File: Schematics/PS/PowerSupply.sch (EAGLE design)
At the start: 32 parts, among them Q1 BUZ10, Q2 BUZ10

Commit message: updates to PS schematic
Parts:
- removed Q1, Q2: BUZ10, transistor-fet:BUZ10
- added C4: (no value), resistor:C-EU025-050X050
- added D6, D7: 1N4933, diode:1N4933
- added R12: (no value), resistor:R-US_0617/22
- added R13, R14: (no value), resistor:R-US_0204/2V
- added T1, T2: IRFP240, Amplifier_Parts:IRFP240
- added TRAFO1: COIL_FORMER, Amplifier_Parts:COIL_FORMER
- R5: device resistor:R-US_0309/12 -> resistor:R-US_0617/22
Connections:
- removed net N$13 (its old number): C1.1, U$5.COM
- new net N$19: D6.C, R13.2, T1.G
- new net N$20: D7.A, R14.1, U$5.LO
- new net N$21: D7.C, R14.2, T2.G
- new net N$22: C2.1, T1.S, T2.D, TRAFO1.P1, U$5.VS
- new net N$9: C4.2, D5.A, R4.1, U$5.VCC
- net N$14: now also D6.A, R13.1, U$5.HO; no longer C2.1, U$5.VS
- net N$4: now also C3.1, R12.2, R4.2, R5.2, U$6.+; no longer D5.A, R4.1, U$5.VCC
- net PE: now also C1.1, C3.2, C4.1, R12.1, R5.1, TRAFO1.P15, TRAFO1.P2, U$5.COM, U$6.-
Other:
- moved on the sheet: C1, C2, D5, R3, R4

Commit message: updates to PS, libary and Action items
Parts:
- removed C16: 1uF, rcl:C-EU025-060X050
- removed D5: 1N4933, diode:1N4933
- removed R12: (no value), resistor:R-US_0617/22
- added C5: 330uF, rcl:CPOL-USE7.5-18
- added R15: 47k, rcl:R-US_0617/5V
- C1, C2: device resistor:C-EU025-050X050 -> rcl:C-EU050-035X075
- C15: device rcl:C-EU025-060X050 -> rcl:C-EU102-064X133
- C17: device rcl:C-EU025-060X050 -> rcl:C-EU075-042X103
- C3: value (none) -> 1uF; device resistor:C-US050-050X075 -> rcl:C-EU102-064X133
- C4: value (none) -> 100uF; device resistor:C-EU025-050X050 -> rcl:CPOL-EUE2.5-6
- D2: value 22V -> 25V; device diode:ZENER-DIODEP1-12 -> diode:ZENER-DIODEP1-Z12
- D3: device diode:ZENER-DIODEDO34-7 -> diode:ZENER-DIODEZD-2.5
- D4: device diode:ZENER-DIODEP1-12 -> diode:ZENER-DIODEP1-Z12
- L1: value RKZ4 -> CHOKE; device inductors:RKZ4 -> Amplifier_Parts:CHOKE
- R1, R7, R8: device resistor:R-US_0207/15 -> rcl:R-US_0204/2V
- R10, R11, R9: device rcl:R-US_0617/22 -> rcl:R-US_0617/5V
- R3: device resistor:R-US_0309/10 -> rcl:R-US_0204/2V
- R4: value (none) -> 47k; device resistor:R-US_0309/10 -> rcl:R-US_0617/5V
- R5: value (none) -> 47k; device resistor:R-US_0617/22 -> rcl:R-US_0617/5V
- R6: device resistor:R-US_0207/15 -> rcl:R-US_0309/V
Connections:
- removed net N$4 (its old number): C3.1, R12.2, R4.2, R5.2, U$6.+
- removed net N$8: C17.2, R10.2, R11.2, R9.2, U$1.NO
- removed net VAC-: C17.1, R10.1, R11.1, R9.1, U$1.COM
- new net N$17: C4.+, R5.1, U$5.VCC
- new net N$24: TRAFO1.S30+1, TRAFO1.SEC30V+
- new net N$25: TRAFO1.GND30
- new net N$26: TRAFO1.S15+1, TRAFO1.SEC15+
- new net N$27: TRAFO1.S15-1, TRAFO1.SEC15-
- new net N$28: TRAFO1.GND15
- new net V+: C5.+, R15.2, R4.2, R5.2, T1.D, U$6.+
- net GND: now also C1.1, C17.1, C5.-, L1.W2E, R10.1, R11.1, R15.1, R4.1, R9.1, T2.S, TRAFO1.P2, TRAFO1.P22, TRAFO1.P23, TRAFO1.P24, TRAFO1.P25, U$1.COM, U$5.COM, U$6.-; no longer C16.2
- net N$10: now also C3.1; no longer C16.1
- net N$14: now also D6.C; no longer D6.A
- net N$18: now also C17.2, R10.2, R11.2, R9.2, U$1.NO; no longer L1.W2E
- net N$19: now also D6.A; no longer D6.C
- net N$20: now also D7.C; no longer D7.A
- net N$21: now also D7.A; no longer D7.C
- net N$22: now also TRAFO1.P12, TRAFO1.P13, TRAFO1.P14, TRAFO1.P15
- net N$6: no longer D5.C
- net N$9: now also TRAFO1.S30-1, TRAFO1.SEC30-; no longer C4.2, D5.A, R4.1, U$5.VCC
- net PE: no longer C1.1, C4.1, R12.1, R5.1, TRAFO1.P15, TRAFO1.P2, U$5.COM, U$6.-
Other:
- note added: "Vac+"
- note added: "check this FP"
- note added: "to mute"
- note removed: "Slow Start Up"
- note removed: "resevoir capacitor - need to decide on value (maybe we can use many in parallel) bledder resistor -we can use the same as the old power supply"
- moved on the sheet: C15, C17, C2, C3, D1, D2, D3, D4, D6, D7, LED2, R1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

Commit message: PS schem updates
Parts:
- added C10, C7, C8, C9: 0.1uF, rcl:C-EU102-064X133
- added C11, C12: 1uF, rcl:C-EU102-064X133
- added C13, C19: 15,000uF, Amplifier_Parts:LNR1K153MSE
- added D10, D5, D8, D9: VS-ETL1506-M3, Amplifier_Parts:VS-ETL1506-M3
- added R12: 100, resistor:R-US_0207/15
- added R16: 2k, rcl:R-US_VTA52
- added R17, R18: 1, rcl:R-US_0411/12
- R2: value 100 -> 2k; device resistor:R-US_0207/15 -> rcl:R-US_VTA52
- R6: value 560 -> 330
- R7: value 390 -> 33; device rcl:R-US_0204/2V -> rcl:R-US_0309/V
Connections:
- net N$24 renamed VAC+40
- net N$26 renamed VAC+15
- net N$27 renamed VAC-15
- net N$9 renamed VAC-40
- removed net N$25: TRAFO1.GND30
- removed net N$28: TRAFO1.GND15
- new net N$23: D5.NC@2, D8.NC@1
- new net N$24: D10.C, D9.A
- new net N$8: C9.2, R17.2
- new net N$9: D5.A, D8.C
- new net SGND: C10.1, C11.2, C12.1, C13.+, C19.-, C7.2, C8.1, R12.1, R16.2, R17.1, R2.1, TRAFO1.GND15, TRAFO1.GND30
- new net VEE: C12.2, C13.-, C8.2, D10.A, D8.A, R16.1, R18.1
- net GND: now also R12.2; no longer R2.1
- net N$10: now also R7.1; no longer R7.2
- net N$11: now also R7.2; no longer R7.1
- net N$3: now also C10.2, R18.2; no longer R2.2, U$3.S2
- net VCC: now also C11.1, C19.+, C7.1, C9.1, D5.C, D9.C, R2.2
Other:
- note added: "check FP"
- note removed: "* we may possibly add the diode bridge rectifier here for the SMPS"
- note removed: "check this FP"
- moved on the sheet: R2, R7, U$3

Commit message: updates to PS
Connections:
- removed net N$24: D10.C, D9.A
- removed net N$9: D5.A, D8.C
- net VAC+40: now also D5.A, D8.C
- net VAC-40: now also D10.C, D9.A
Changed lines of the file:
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@@
 <junction x="177.8" y="60.96"/>
+</segment>
+<segment>
+<pinref part="D5" gate="G$1" pin="A"/>
+<wire x1="88.9" y1="22.86" x2="83.82" y2="22.86" width="0.1524" layer="91"/>
+<pinref part="D8" gate="G$1" pin="C"/>
+<wire x1="83.82" y1="22.86" x2="63.5" y2="22.86" width="0.1524" layer="91"/>
+<wire x1="83.82" y1="20.32" x2="83.82" y2="22.86" width="0.1524" layer="91"/>
+<junction x="83.82" y="22.86"/>
 </segment>
 </net>
@@
 <wire x1="182.88" y1="53.34" x2="177.8" y2="53.34" width="0.1524" layer="91"/>
 <junction x="177.8" y="53.34"/>
+</segment>
+<segment>
+<wire x1="63.5" y1="10.16" x2="99.06" y2="10.16" width="0.1524" layer="91"/>
+<pinref part="D9" gate="G$1" pin="A"/>
+<wire x1="99.06" y1="10.16" x2="99.06" y2="12.7" width="0.1524" layer="91"/>
+<wire x1="99.06" y1="15.24" x2="99.06" y2="12.7" width="0.1524" layer="91"/>
+<pinref part="D10" gate="G$1" pin="C"/>
+<wire x1="99.06" y1="12.7" x2="93.98" y2="12.7" width="0.1524" layer="91"/>
+<junction x="99.06" y="12.7"/>
 </segment>
 </net>
@@
 <wire x1="83.82" y1="-17.78" x2="106.68" y2="-17.78" width="0.1524" layer="91"/>
 <junction x="106.68" y="-17.78"/>
+<junction x="83.82" y="12.7"/>
 </segment>
 </net>
@@
 </segment>
 </net>
-<net name="N$9" class="0">
-<segment>
-<pinref part="D5" gate="G$1" pin="A"/>
-<wire x1="88.9" y1="22.86" x2="83.82" y2="22.86" width="0.1524" layer="91"/>
-<pinref part="D8" gate="G$1" pin="C"/>
-<wire x1="83.82" y1="22.86" x2="63.5" y2="22.86" width="0.1524" layer="91"/>
-<wire x1="83.82" y1="20.32" x2="83.82" y2="22.86" width="0.1524" layer="91"/>
-<junction x="83.82" y="22.86"/>
-</segment>
-</net>
-<net name="N$24" class="0">
-<segment>
-<wire x1="63.5" y1="10.16" x2="99.06" y2="10.16" width="0.1524" layer="91"/>
-<pinref part="D9" gate="G$1" pin="A"/>
-<wire x1="99.06" y1="10.16" x2="99.06" y2="12.7" width="0.1524" layer="91"/>
-<wire x1="99.06" y1="15.24" x2="99.06" y2="12.7" width="0.1524" layer="91"/>
-<pinref part="D10" gate="G$1" pin="C"/>
-<wire x1="99.06" y1="12.7" x2="93.98" y2="12.7" width="0.1524" layer="91"/>
-<junction x="99.06" y="12.7"/>
-</segment>
-</net>

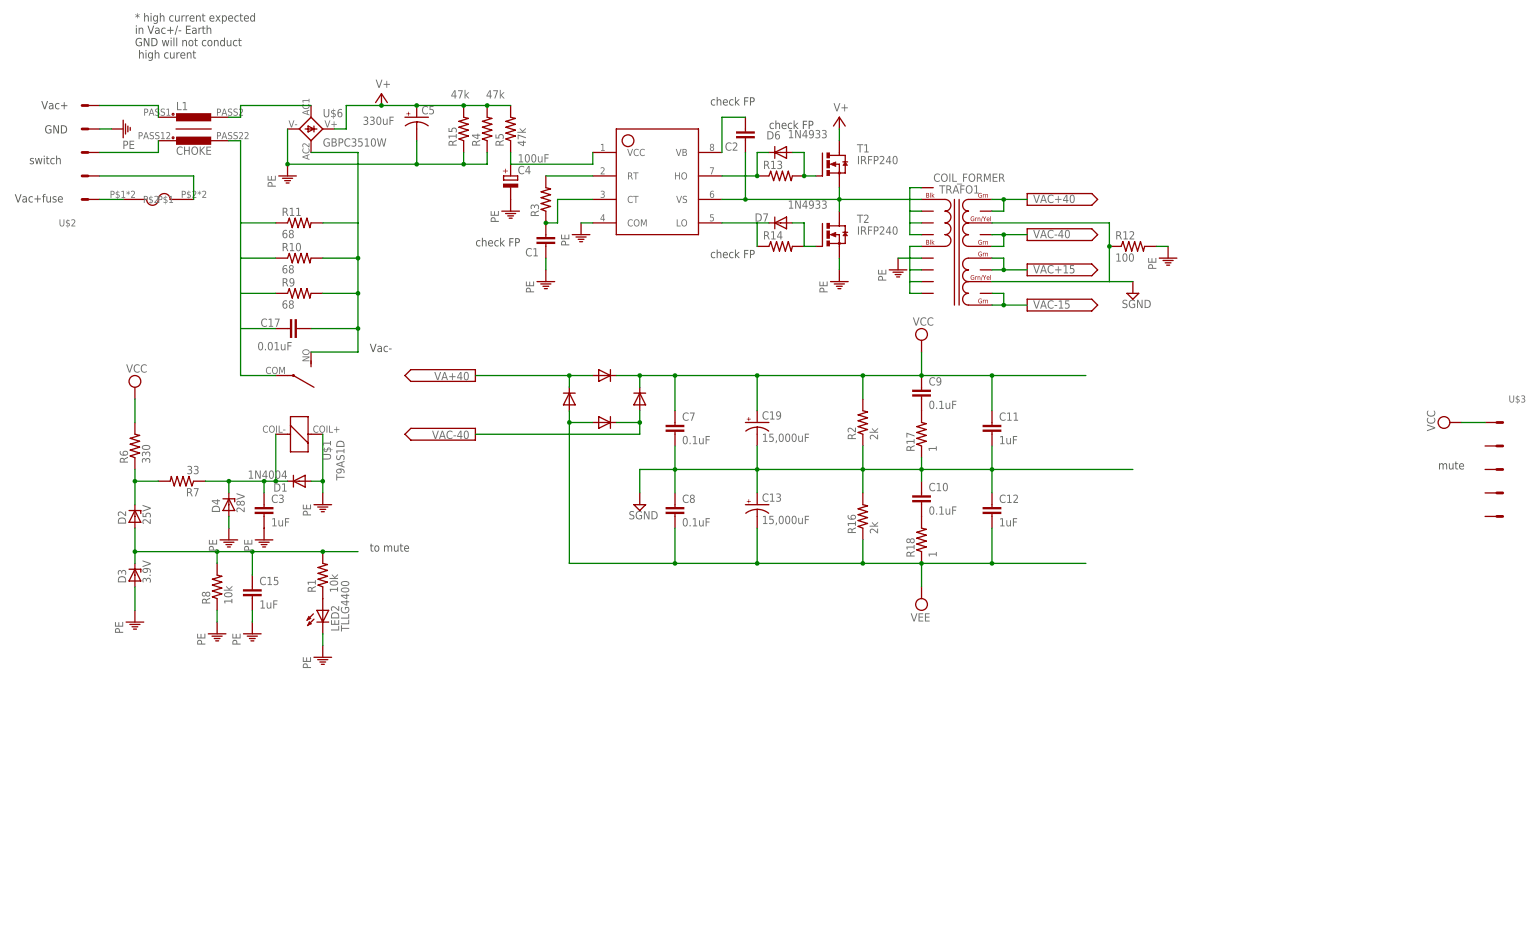
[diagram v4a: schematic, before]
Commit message: updates to PS schematic, created special 1N4004 part
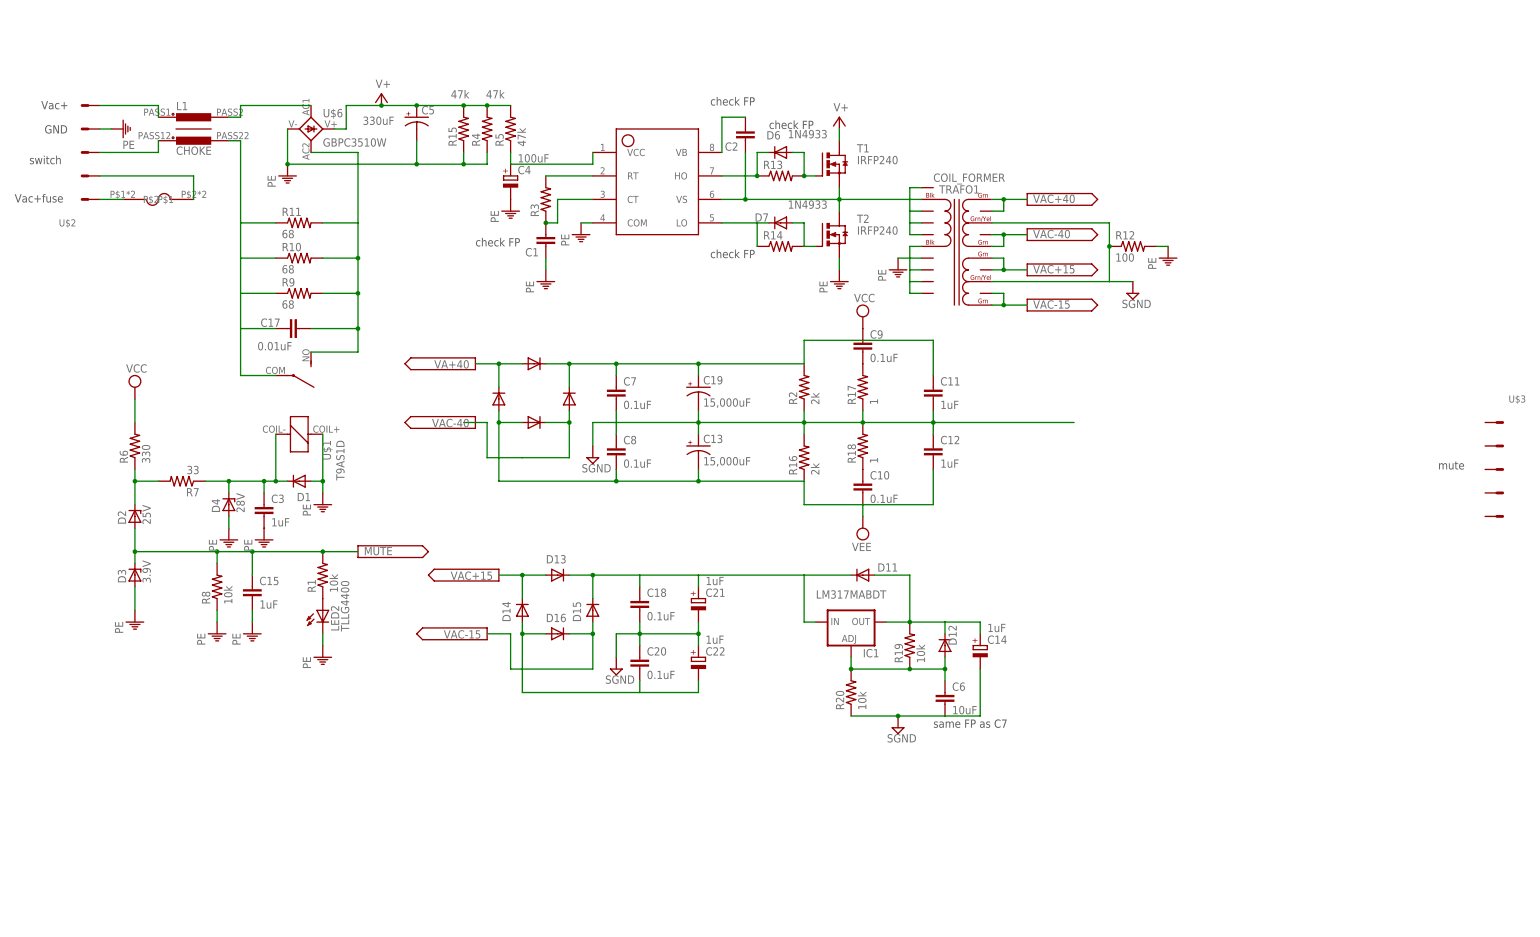
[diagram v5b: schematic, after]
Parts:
- added C14, C21, C22: 1uF, rcl:CPOL-EUE2.5-6
- added C18, C20: 0.1uF, rcl:C-EU102-064X133
- added C6: 10uF, rcl:C-EU102-064X133
- added D11, D12, D13, D14, D15, D16: 1N4004, Amplifier_Parts:1N4004
- added IC1: LM317MABDT, v-reg:LM317MABDT
- added R19, R20: 10k, rcl:R-US_0204/2V
- D1: device diode:1N4004 -> Amplifier_Parts:1N4004
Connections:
- net N$12 renamed MUTE
- removed net N$3: C10.2, R18.2
- new net N$25: C10.1, R18.1
- new net N$26: C6.1, D12.A, IC1.ADJ, R19.1, R20.2
- new net VCC1: C18.1, C21.+, D11.C, D13.C, D15.C, IC1.IN
- new net VEE1: C20.2, C22.-, D14.A, D16.A
- net N$23: now also C14.+, D11.A, D12.C, IC1.OUT, R19.2; no longer D5.NC@2, D8.NC@1
- net SGND: now also C14.-, C18.2, C20.1, C21.-, C22.+, C6.2, R18.2, R20.1; no longer C10.1
- net VAC+15: now also D13.A, D14.C
- net VAC-15: now also D15.A, D16.C
- net VAC-40: now also D10.NC@2
- net VCC: no longer U$3.S1
- net VEE: now also C10.2; no longer R18.1
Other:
- note added: "same FP as C7"
- note removed: "* high current expected in Vac+/- Earth GND will not conduct high curent"
- note removed: "Vac-"
- note removed: "to mute"
- moved on the sheet: C10, C11, C12, C13, C19, C7, C8, C9, R16, R17, R18, R2

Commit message: updates to PS, it is finished
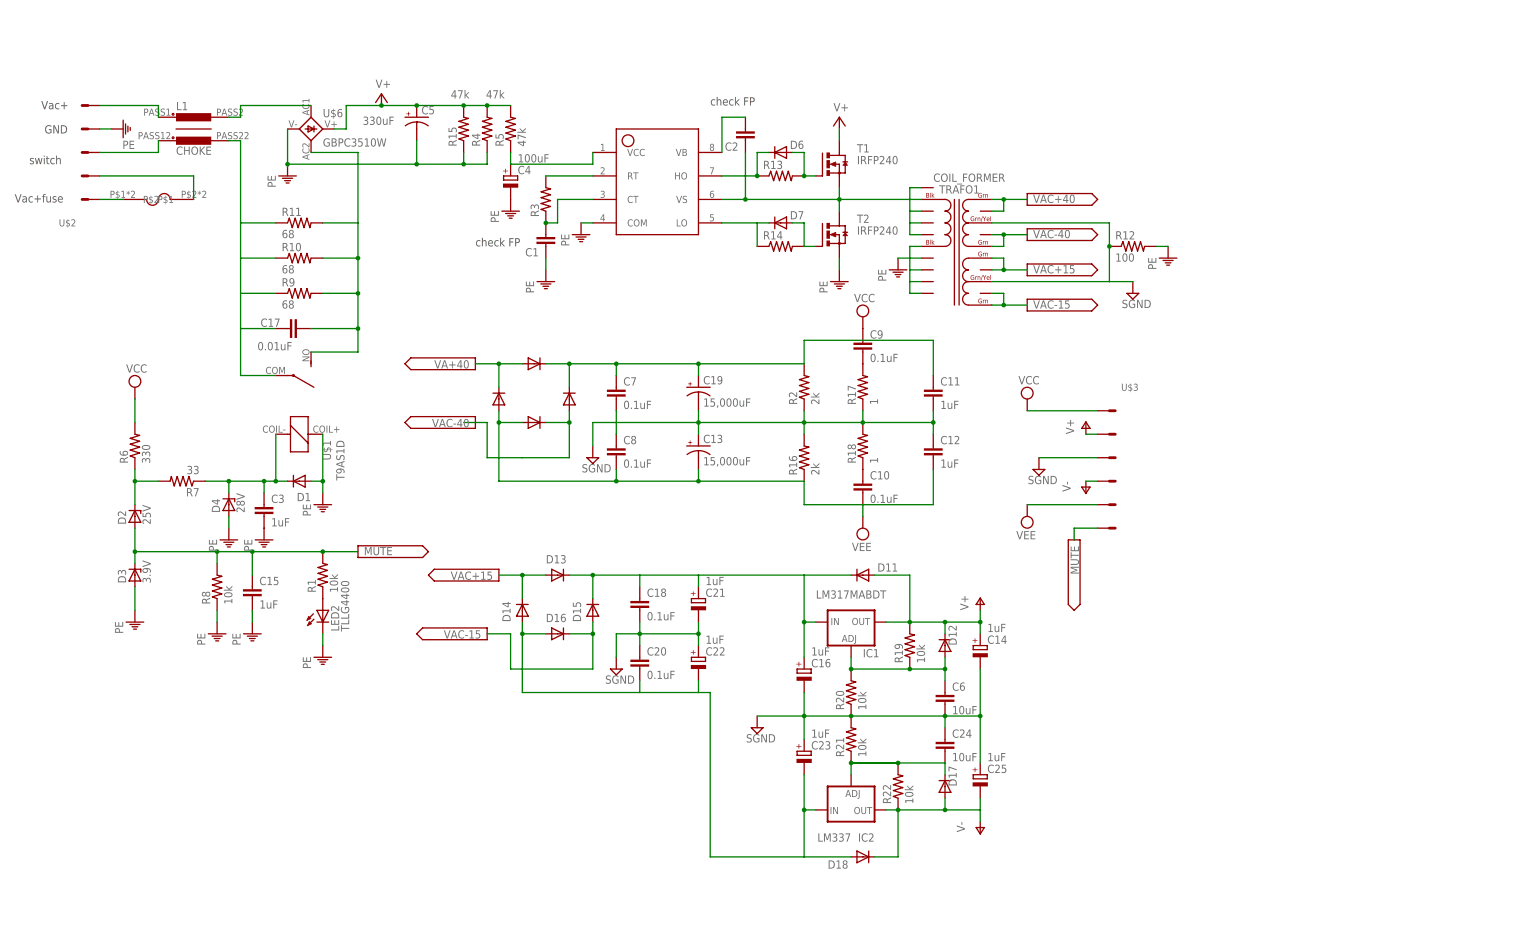
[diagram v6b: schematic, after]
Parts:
- added C16, C23, C25: 1uF, rcl:CPOL-EUE2.5-6
- added C24: 10uF, resistor:C-EU025-025X050
- added D17, D18: 1N4004, Amplifier_Parts:1N4004
- added IC2: LM337, Amplifier_Parts:LM337
- added R21, R22: 10k, rcl:R-US_0204/2V
- C1: device rcl:C-EU050-035X075 -> resistor:C-EU025-025X050
- C6: device rcl:C-EU102-064X133 -> resistor:C-EU025-025X050
- D6, D7: value 1N4933 -> 1N4004; device diode:1N4933 -> Amplifier_Parts:1N4004
- U$3: value SCREW_TERMINAL_5 -> SCREW_TERMINAL_6; device Amplifier_Parts:SCREW_TERMINAL_5 -> Amplifier_Parts:SCREW_TERMINAL_6
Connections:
- removed net N$23: C14.+, D11.A, D12.C, IC1.OUT, R19.2
- removed net VCC1: C18.1, C21.+, D11.C, D13.C, D15.C, IC1.IN
- removed net VEE1: C20.2, C22.-, D14.A, D16.A
- new net N$3: C24.2, D17.C, IC2.ADJ, R21.1, R22.2
- new net V-: C25.-
- new net V-15UN: C20.2, C22.-, C23.-, D14.A, D16.A, D18.A, IC2.IN
- new net V15+: C14.+, D11.A, D12.C, IC1.OUT, R19.2, U$3.S2
- new net V15-: D17.A, D18.C, IC2.OUT, R22.1, U$3.S4
- new net V15UN: C16.+, C18.1, C21.+, D11.C, D13.C, D15.C, IC1.IN
- net GND: now also U$2.S4
- net MUTE: now also U$3.S6
- net PE: no longer U$2.S4
- net SGND: now also C16.-, C23.+, C24.1, C25.+, R21.2, U$3.S3
- net VCC: now also U$3.S1
- net VEE: now also U$3.S5
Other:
- note removed: "mute"
- note removed: "same FP as C7"
